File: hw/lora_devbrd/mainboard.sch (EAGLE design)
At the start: 5 parts, among them U1 RHF78-052

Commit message: Adds FT232RL
TODO:
        * add LM1117/SOT-23
        * trace board
        * check, check, check
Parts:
- added C1: 100nf, rcl:C-EUC1206
- added C2: 100nF, rcl:C-EUC1206
- added IC1: FT232RL, ftdichip:FT232RL
- added JP1: (no value), jumper:JP1E
- added LED1, LED2: (no value), led:LEDCHIPLED_1206
- added R1, R2, R3: (no value), rcl:R-EU_M1206
- added S1: DTSM-6, switch-tact:DTSM-6
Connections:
- new net N$1: C1.2, IC1.3V3OUT
- new net N$5: IC1.CBUS0, LED1.C
- new net N$6: IC1.CBUS1, LED2.C
- new net N$7: LED1.A, R1.1
- new net N$9: LED2.A, R2.1
- new net RXD: IC1.RXD, JP1.1
- new net TXD: IC1.TXD, JP1.2
- net 5V: now also R1.2, R2.2
- net D+: now also IC1.USBDP
- net D-: now also IC1.USBDM
- net GND: now also C1.1, C2.1, IC1.GND, IC1.GND@1, IC1.GND@2, IC1.GND@A, S1.3
- net NRST: now also R3.1, S1.1
- net VCC: now also C2.2, IC1.VCC, IC1.VCCIO, R3.2

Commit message: Adds LM1117
TODO:
            * trace board
            * check, check, check
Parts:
- added C3, C4: (no value), rcl:C-USC1206
- added IC2: LM1117MP-3.3, lm1117_10:LM1117MP-3.3
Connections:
- net 5V: now also C3.1, IC2.IN; no longer R1.2, R2.2
- net GND: now also C3.2, C4.2, IC2.GND
- net VCC: now also C4.1, IC2.OUT, R1.2, R2.2
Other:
- moved on the sheet: C1, C2, IC1, JP1, LED1, LED2, R1, R2, R3, S1, SV1, U$1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

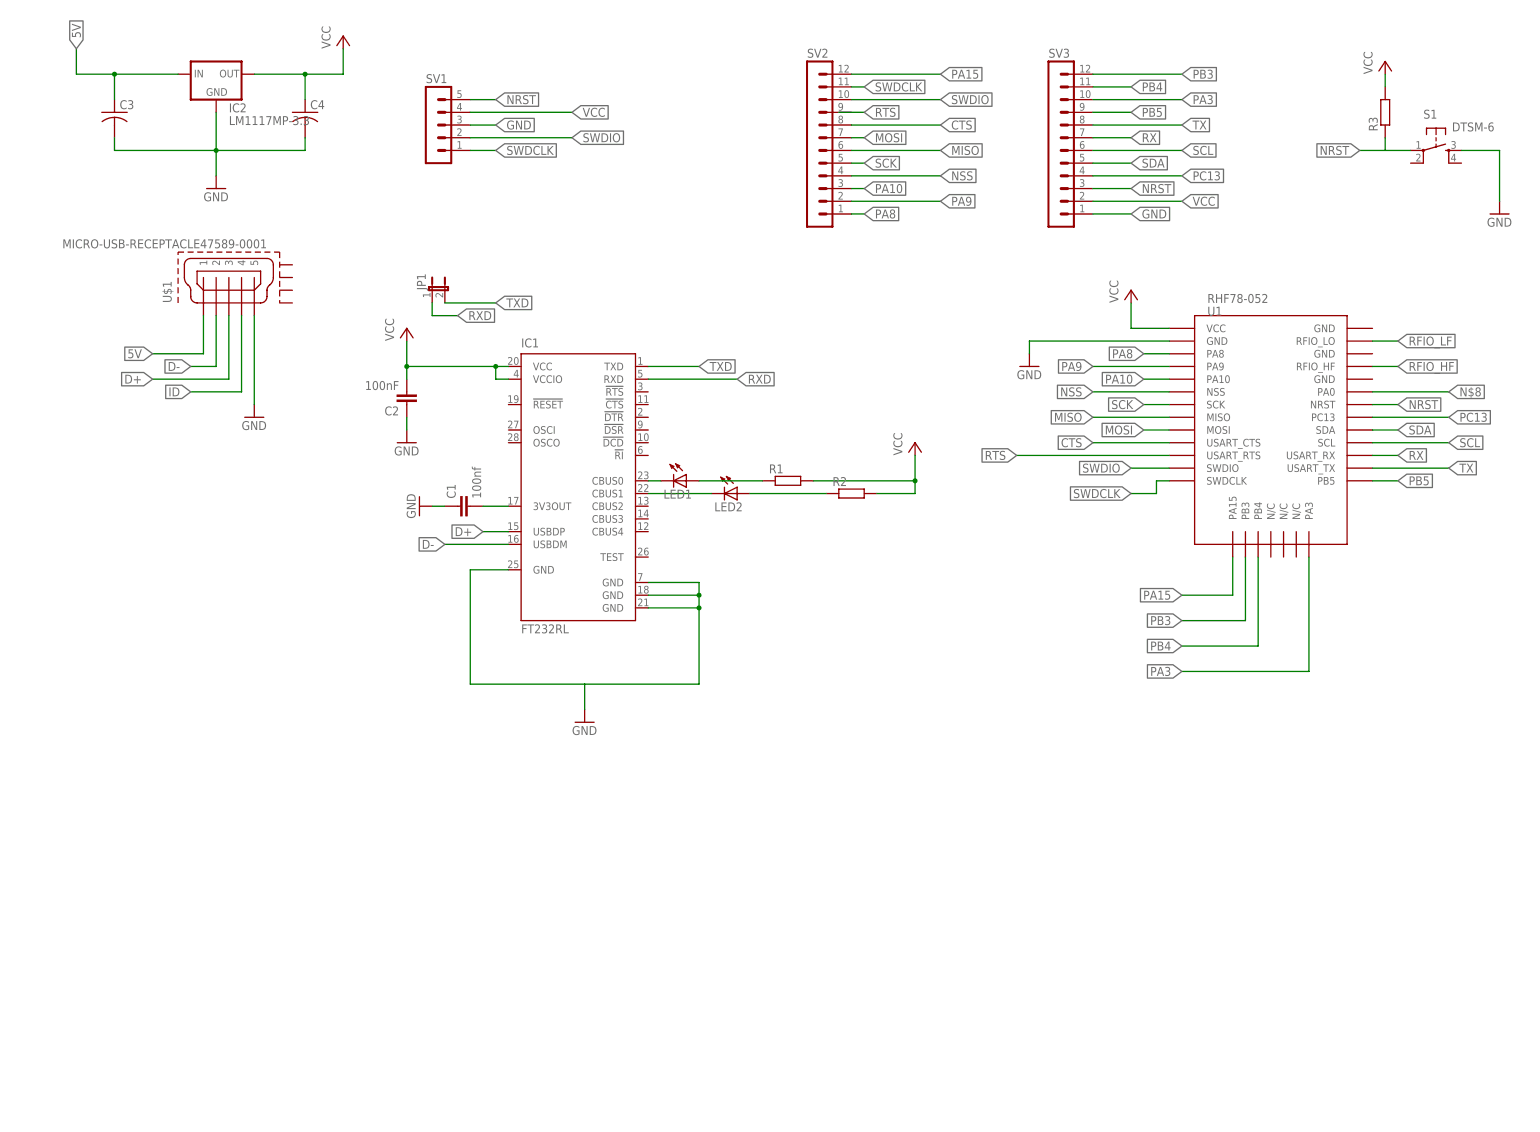
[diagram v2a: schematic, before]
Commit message: Adds some leds for power, rx/tx and custom indication
    TODO:
                * trace board
                * check footprints
                * check, check, check
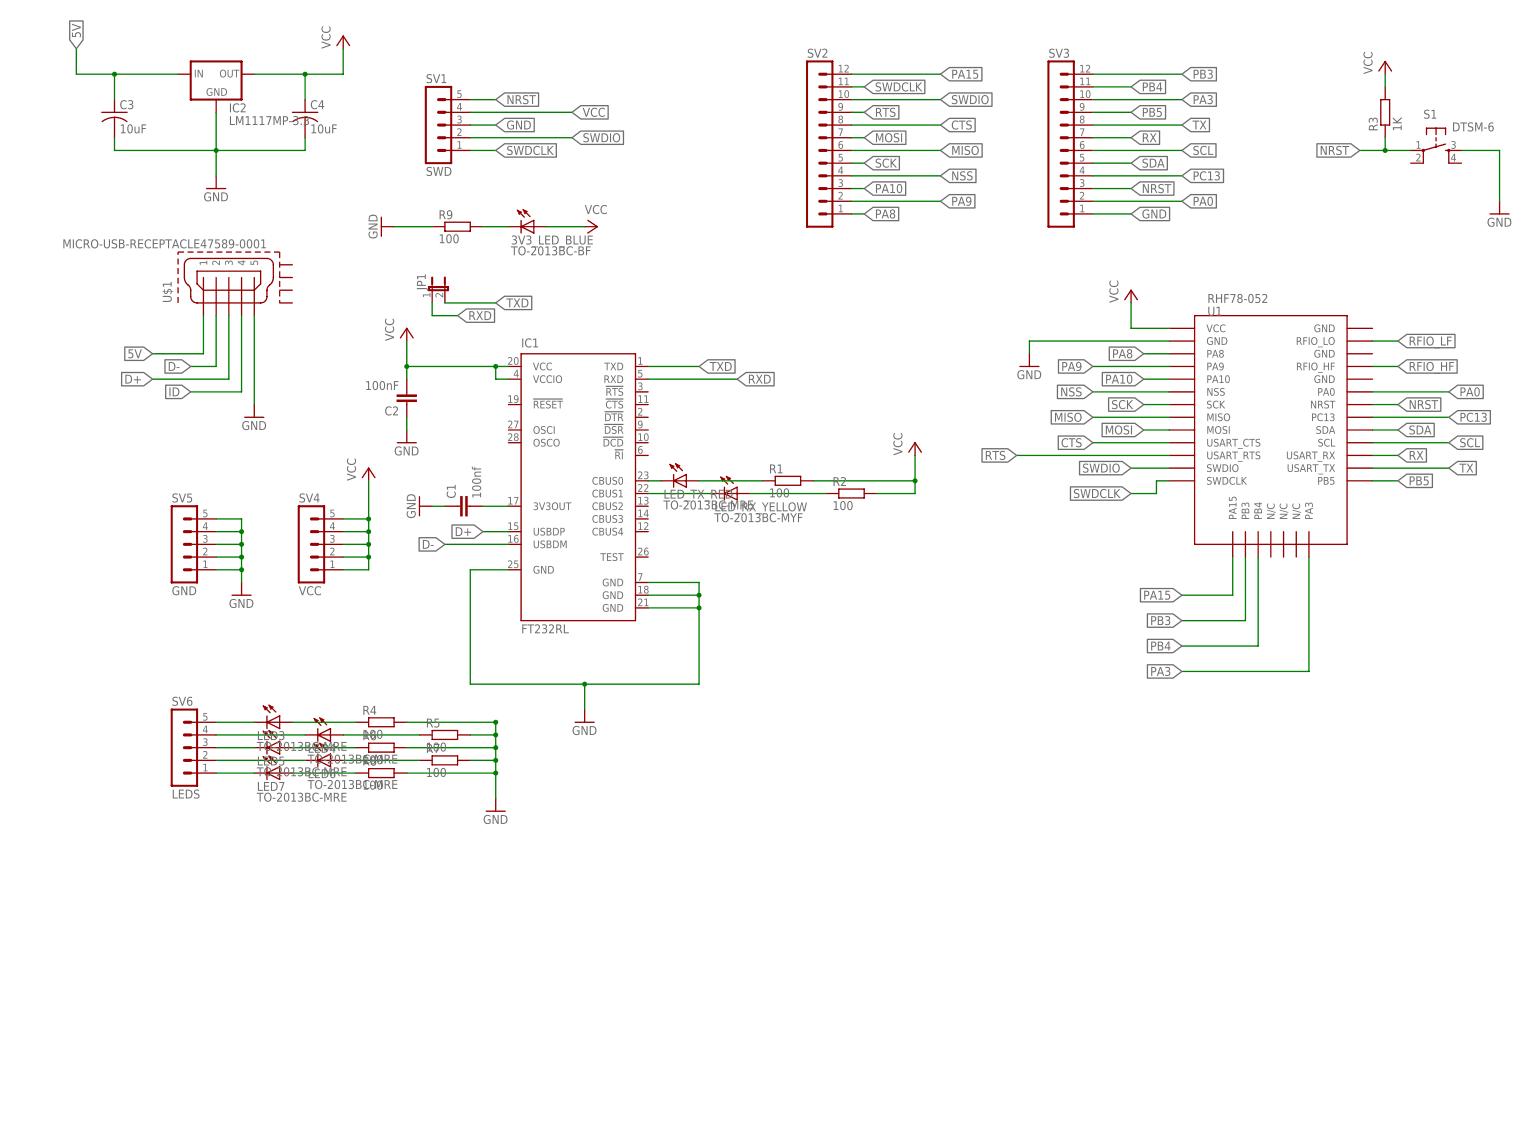
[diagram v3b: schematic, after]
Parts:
- added 3V3_LED_BLUE: TO-2013BC-BF, led:LEDCHIPLED_1206
- added LED3, LED4, LED5, LED6, LED7: TO-2013BC-MRE, led:LEDCHIPLED_1206
- added R4, R5, R6, R7, R8, R9: 100, rcl:R-EU_M1206
- added SV4: VCC, con-lstb:MA05-1
- added SV5: GND, con-lstb:MA05-1
- added SV6: LEDS, con-lstb:MA05-1
- C3, C4: value (none) -> 10uF
- LED_RX_YELLOW: value (none) -> TO-2013BC-MYF
- LED_TX_RED: value (none) -> TO-2013BC-MRE
- R1, R2: value (none) -> 100
- R3: value (none) -> 1K
- SV1: value (none) -> SWD
- renumbered LED1 to LED_TX_RED, LED2 to LED_RX_YELLOW
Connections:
- removed net N$8: U1.PA0
- new net N$12: LED3.C, SV6.5
- new net N$13: LED4.C, SV6.4
- new net N$14: LED5.C, SV6.3
- new net N$15: LED6.C, SV6.2
- new net N$16: LED7.C, SV6.1
- new net N$17: LED3.A, R4.1
- new net N$18: LED4.A, R5.1
- new net N$19: LED5.A, R6.1
- new net N$2: 3V3_LED_BLUE.C, R9.2
- new net N$20: LED6.A, R7.1
- new net N$21: LED7.A, R8.1
- new net PA0: SV3.2, U1.PA0
- net GND: now also R4.2, R5.2, R6.2, R7.2, R8.2, R9.1, SV5.1, SV5.2, SV5.3, SV5.4, SV5.5
- net RTS: now also SV2.9
- net VCC: now also 3V3_LED_BLUE.A, SV4.1, SV4.2, SV4.3, SV4.4, SV4.5; no longer SV3.2

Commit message: WIP: tracing
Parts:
- added C5: 100nF, rcl:C-EUC1206
- R1, R2, R3, R4, R5, R6, R7, R8, R9: device rcl:R-EU_M1206 -> rcl:R-EU_R1206
- renumbered JP1 to USART
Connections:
- net N$1 renamed 3V3OUT
- net N$5 renamed CBUS0
- net N$6 renamed CBUS1
- net GND: now also C5.1
- net VCC: now also C5.2
